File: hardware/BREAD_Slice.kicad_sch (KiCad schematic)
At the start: 20 parts, among them J1 I2C_01x04, J2 Conn_01x10_Female, J3 Screw_Terminal_01x04, J4 Screw_Terminal_01x03, J5 Screw_Terminal_01x03, J6 Screw_Terminal_01x03, J7 Screw_Terminal_01x03

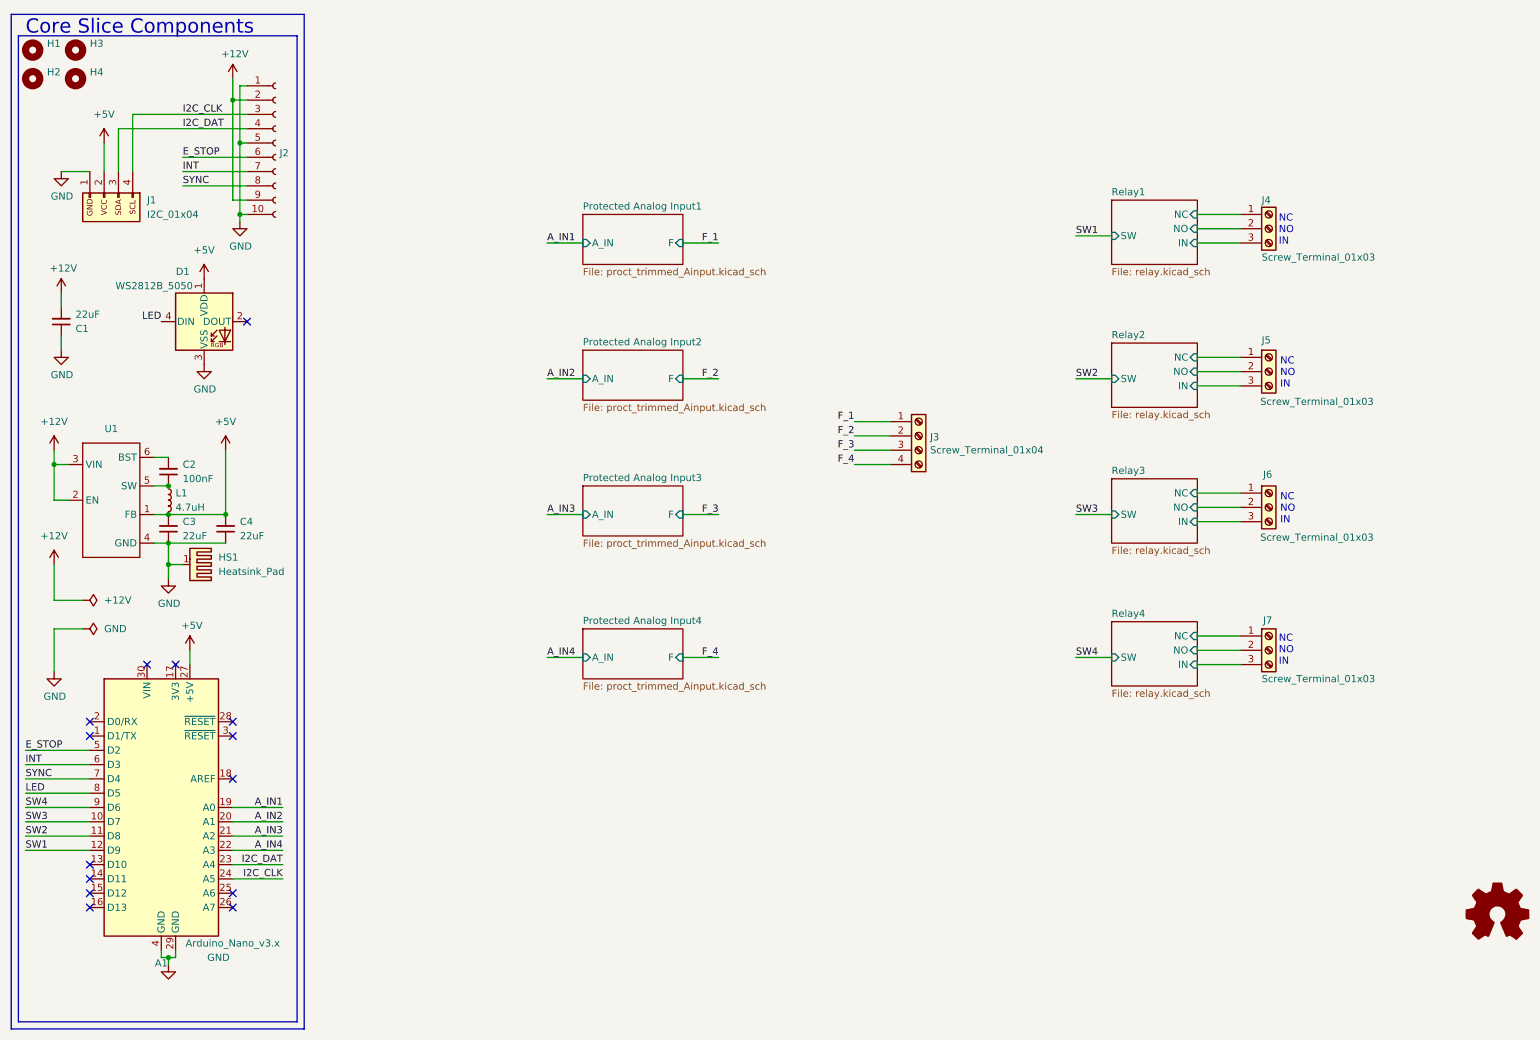
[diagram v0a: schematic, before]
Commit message: update to use latest kmlib; needs revision for connectors and ground inputs on analog inputs
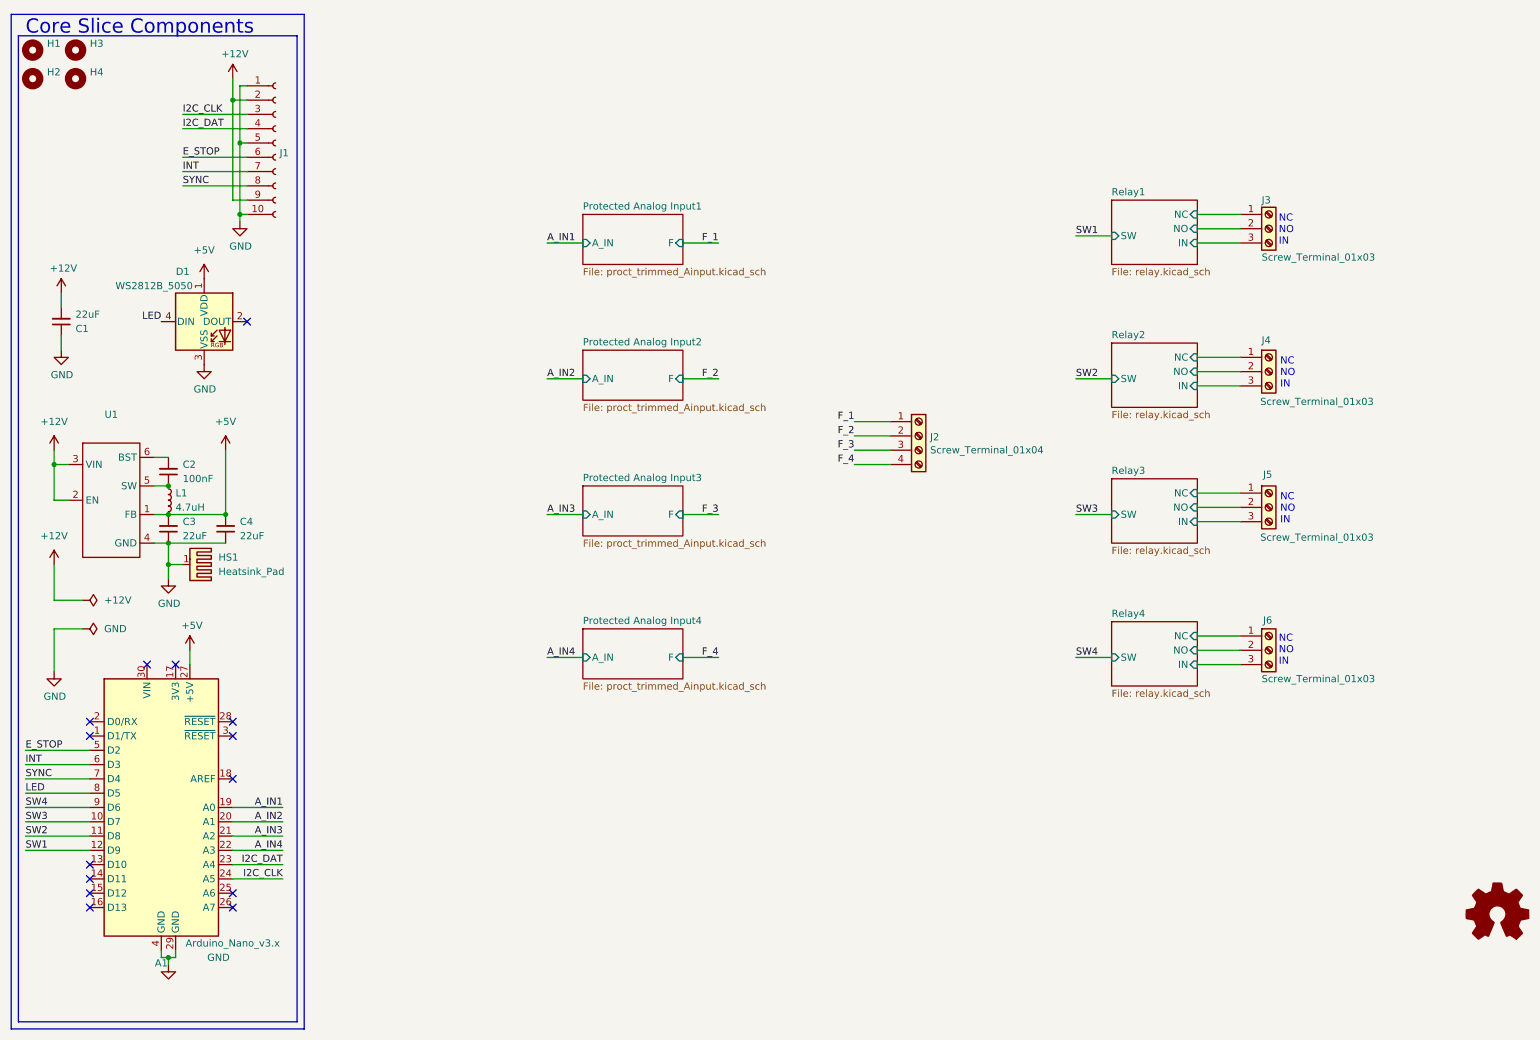
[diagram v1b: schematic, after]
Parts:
- removed J1: I2C_01x04, Connector_JST:JST_SH_SM04B-SRSS-TB_1x04-1MP_P1.00mm_Horizontal, symbol SparkFun-Connector:I2C_01x04
- A1: footprint Module:Arduino_Nano -> KMLib_Boards_Modules:Arduino_Nano; symbol MCU_Module:Arduino_Nano_v3.x -> KMLib_IC_MCU_MPU:Arduino_Nano_v3.x
- D1: footprint SparkFun-LED:WS2812-5050-4PIN -> KMLib_IC_SMD:WS2812-5050-4PIN; symbol SparkFun-LED:WS2812B_5050 -> KMLib_IC_Digital:WS2812B_5050_RGB_LED; PROD_ID (none) -> DIO-12503
- HS1: footprint KML-Custom:Thermal Pad -> KMLib_Mounting:Thermal Pad
- J1: renamed from J2; symbol Connector:Conn_01x10_Female -> Connector:Conn_01x10_Socket
- U1: footprint Package_TO_SOT_SMD:TSOT-23-6 -> KMLib_IC_SMD:SOIC_05WU-7_DIO; symbol SparkFun-DiscreteSemi:AP63205 -> KMLib_IC_Power:AP63205WU-7_Buck_Regulator
- renumbered J3 to J2, J4 to J3, J5 to J4, J6 to J5, J7 to J6
